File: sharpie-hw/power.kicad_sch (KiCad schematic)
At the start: 21 parts, among them J2 Conn_01x02_MountingPin, J5 Conn_01x14, J6 LS021B7DD02, U1 TPS7A2533, U2 TPS7A2501, U7 AP3602A

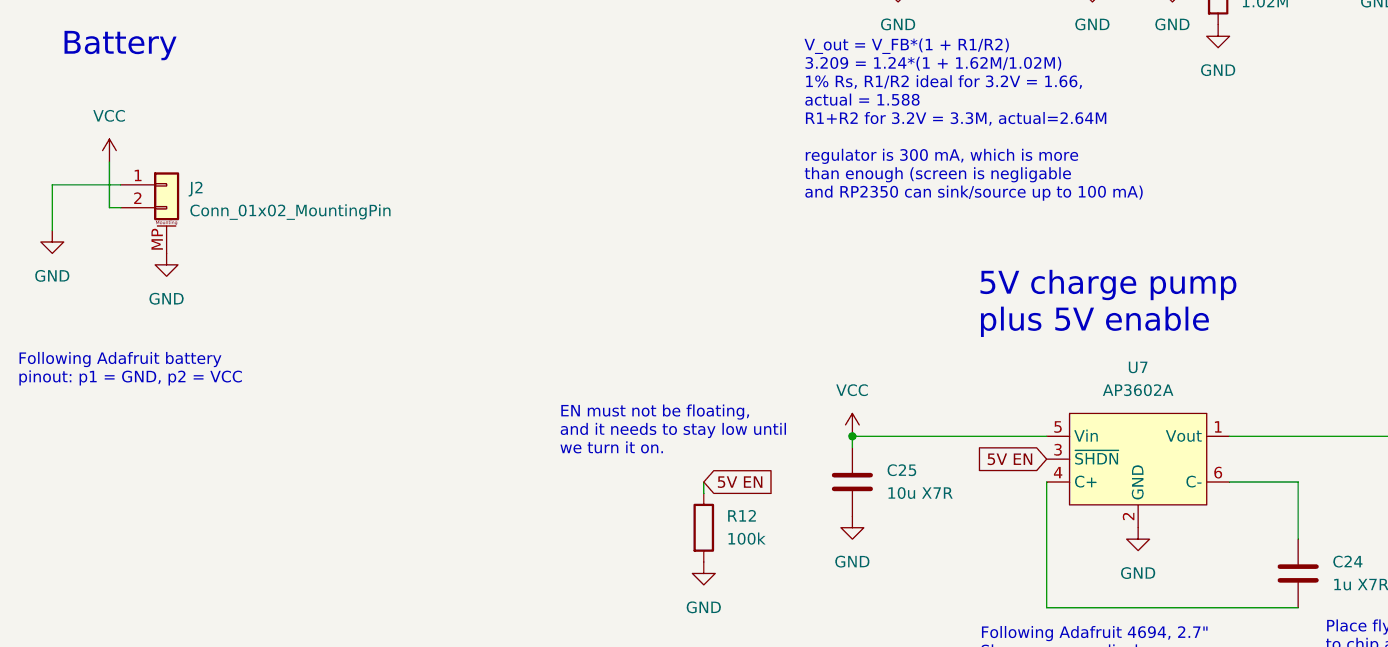
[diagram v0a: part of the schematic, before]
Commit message: Fix two items: battery connector polarity and AP3602 capacitor polarity.
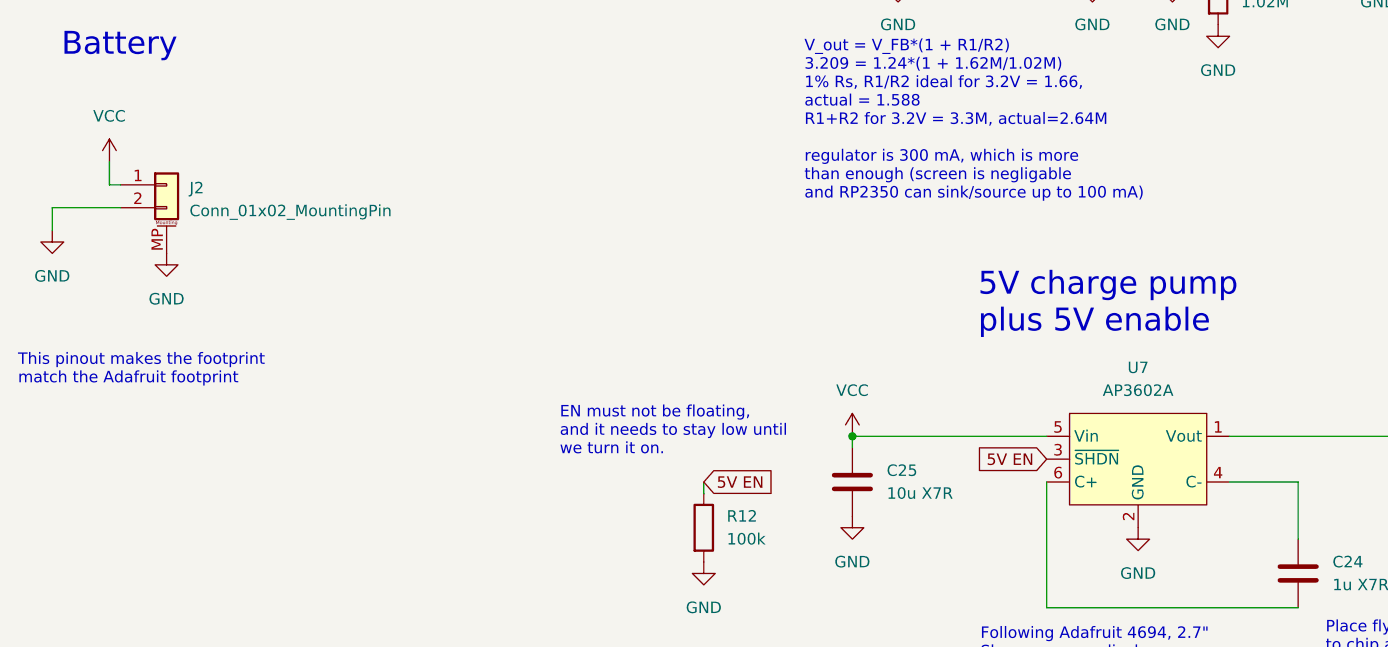
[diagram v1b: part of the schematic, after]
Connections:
- net GND: now also J2.2 (Pin_2); no longer J2.1 (Pin_1)
- net VCC: now also J2.1 (Pin_1); no longer J2.2 (Pin_2)
- net at C24.1: now also U7.6 (C+); no longer U7.4 (C+)
- net at C24.2: now also U7.4 (C-); no longer U7.6 (C-)
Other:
- note added: "This pinout makes the footprint match the Adafruit footprint"
- note removed: "Following Adafruit battery pinout: p1 = GND, p2 = VCC"
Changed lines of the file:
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@@
 		)
 	)
-	(text "Following Adafruit battery\npinout: p1 = GND, p2 = VCC"
+	(text "This pinout makes the footprint\nmatch the Adafruit footprint"
 		(exclude_from_sim no)
 		(at 19.05 134.874 0)
@@
 	(wire
 		(pts
-			(xy 22.86 114.3) (xy 22.86 119.38)
+			(xy 29.21 114.3) (xy 30.48 114.3)
 		)
 		(stroke
@@
 	(wire
 		(pts
+			(xy 29.21 111.76) (xy 29.21 114.3)
+		)
+		(stroke
+			(width 0)
+			(type default)
+		)
+	)
+	(wire
+		(pts
 			(xy 66.04 36.83) (xy 66.04 41.91)
 		)
@@
 	(wire
 		(pts
-			(xy 29.21 116.84) (xy 29.21 111.76)
-		)
-		(stroke
-			(width 0)
-			(type default)
-		)
-	)
-	(wire
-		(pts
 			(xy 95.25 147.32) (xy 95.25 148.59)
 		)
@@
 	(wire
 		(pts
-			(xy 30.48 114.3) (xy 22.86 114.3)
-		)
-		(stroke
-			(width 0)
-			(type default)
-		)
-	)
-	(wire
-		(pts
 			(xy 137.16 50.8) (xy 138.43 50.8)
 		)
@@
 	(wire
 		(pts
+			(xy 22.86 116.84) (xy 22.86 119.38)
+		)
+		(stroke
+			(width 0)
+			(type default)
+		)
+	)
+	(wire
+		(pts
 			(xy 137.16 91.44) (xy 138.43 91.44)
 		)
@@
 	(wire
 		(pts
-			(xy 30.48 116.84) (xy 29.21 116.84)
-		)
-		(stroke
-			(width 0)
-			(type default)
-		)
-	)
-	(wire
-		(pts
 			(xy 116.84 46.99) (xy 116.84 50.8)
 		)
@@
 		)
 		(stroke
+			(width 0)
+			(type default)
+		)
+	)
+	(wire
+		(pts
+			(xy 30.48 116.84) (xy 22.86 116.84)
+		)
+		(stroke

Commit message: PCB changes of some kind: appears to be the version sent to JLC.
The manufactured version of the PCB has no voltage divider or battery input,
because they were unnecssary (and in the case of the battery input,
unsafe).
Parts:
- removed J2: Conn_01x02_MountingPin, Connector_JST:JST_PH_S2B-PH-SM4-TB_1x02-1MP_P2.00mm_Horizontal, symbol Connector_Generic_MountingPin:Conn_01x02_MountingPin
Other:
- note removed: "Battery"
- note removed: "This pinout makes the footprint match the Adafruit footprint"
